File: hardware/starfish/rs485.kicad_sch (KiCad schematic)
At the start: 4 parts, among them J801 Feeders, U801 MAX3078E

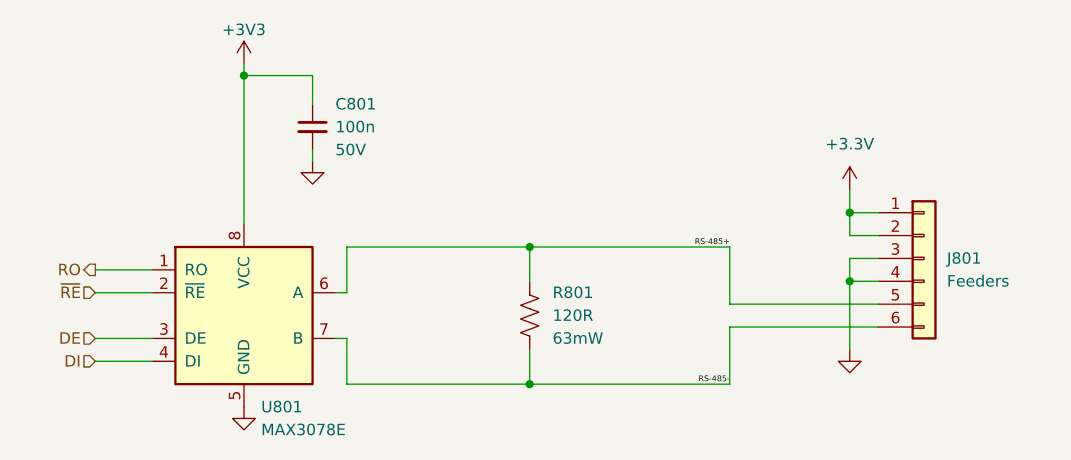
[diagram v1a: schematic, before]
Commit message: starfish: remove feeder header and use screw terminals for rs-485
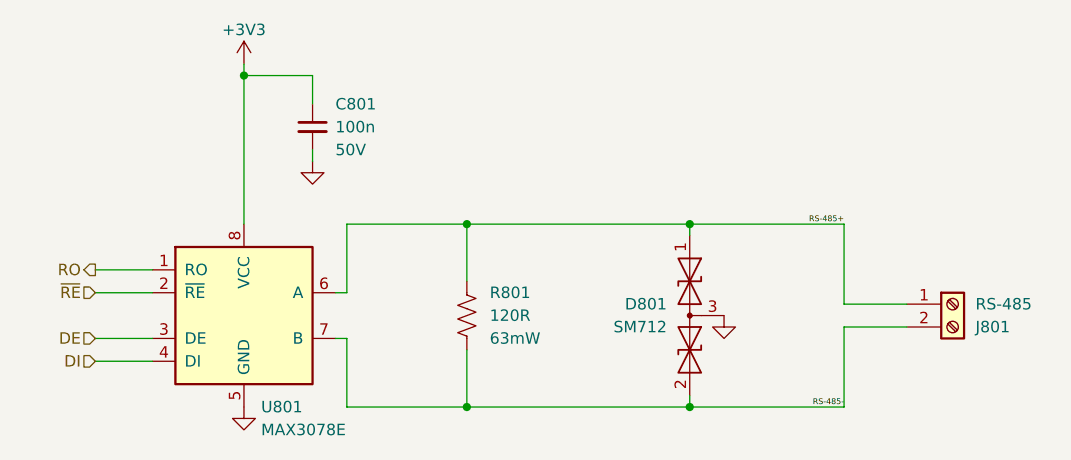
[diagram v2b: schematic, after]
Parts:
- removed J801: Feeders, Connector_IDC:IDC-Header_2x03_P2.54mm_Vertical, symbol Connector_Generic:Conn_01x06
- added D801: SM712, Package_TO_SOT_SMD:SOT-23, symbol Diode:SM712_SOT23
- added J801: RS-485, winterbloom:TerminalBlock_4UCON_1x02_P3.50mm_Horizontal, symbol Connector:Screw_Terminal_01x02
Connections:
- net GND: now also D801.3 (common)
- net RS-485+: now also D801.1 (A1), J801.1 (Pin_1)
- net RS-485-: now also D801.2 (A2), J801.2 (Pin_2)
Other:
- moved on the sheet: R801
